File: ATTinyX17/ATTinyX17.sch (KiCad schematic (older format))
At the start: 27 parts, among them J1 Conn_01x13, J2 Conn_01x13, J4 UPDI, SW1 RST, U1 AP7365, U2 ATtiny3217-M

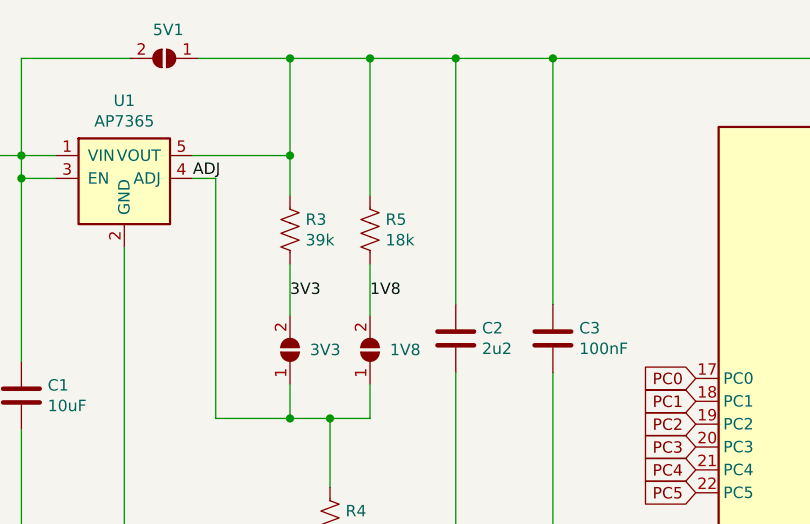
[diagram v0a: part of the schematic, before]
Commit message: SirTiny X1X Revisions
18k Changed to 16k
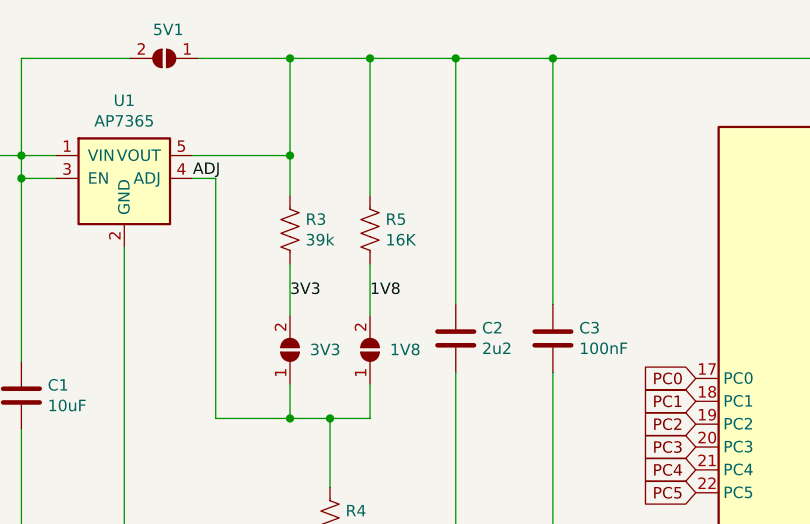
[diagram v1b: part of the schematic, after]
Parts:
- R5: value 18k -> 16K; Part C304766 -> C4210
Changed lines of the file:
@@
 P 3100 1525
 F 0 "R5" H 3168 1570 50  0000 L CNN
-F 1 "18k" H 3168 1480 50  0000 L CNN
+F 1 "16K" H 3168 1480 50  0000 L CNN
 F 2 "Resistor_SMD:R_0603_1608Metric" V 3140 1515 50  0001 C CNN
 F 3 "~" H 3100 1525 50  0001 C CNN
-F 4 "C304766" H 3100 1525 50  0001 C CNN "Part"
+F 4 "C4210" H 3100 1525 50  0001 C CNN "Part"
 	1    3100 1525
 	1    0    0    -1
